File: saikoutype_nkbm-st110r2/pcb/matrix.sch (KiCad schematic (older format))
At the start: 239 parts, among them K00 CHRY_MX, K02 CHRY_MX, K03 CHRY_MX, K04 CHRY_MX, K05 CHRY_MX, K06 CHRY_MX, K07 CHRY_MX, K08 CHRY_MX, K09 CHRY_MX, K0B CHRY_MX, K0C CHRY_MX, K0D CHRY_MX, K0E CHRY_MX, K1A? CHRY_MX, K1B? CHRY_MX, K1C? CHRY_MX, K1D? CHRY_MX, K1E? CHRY_MX, K2A? CHRY_MX, K2B? CHRY_MX, K2C? CHRY_MX, K3A? CHRY_MX, K3B? CHRY_MX, K3C? CHRY_MX, K3E? CHRY_MX, K4A? CHRY_MX, K4B? CHRY_MX, K4C? CHRY_MX, K4D? CHRY_MX, K5A? CHRY_MX, K5D? CHRY_MX, K5E? CHRY_MX, K6A? CHRY_MX, K6B? CHRY_MX, K6C? CHRY_MX, K6D? CHRY_MX, K6E? CHRY_MX, K7A? CHRY_MX, K7B? CHRY_MX, K7C? CHRY_MX, K7D? CHRY_MX, K7E? CHRY_MX

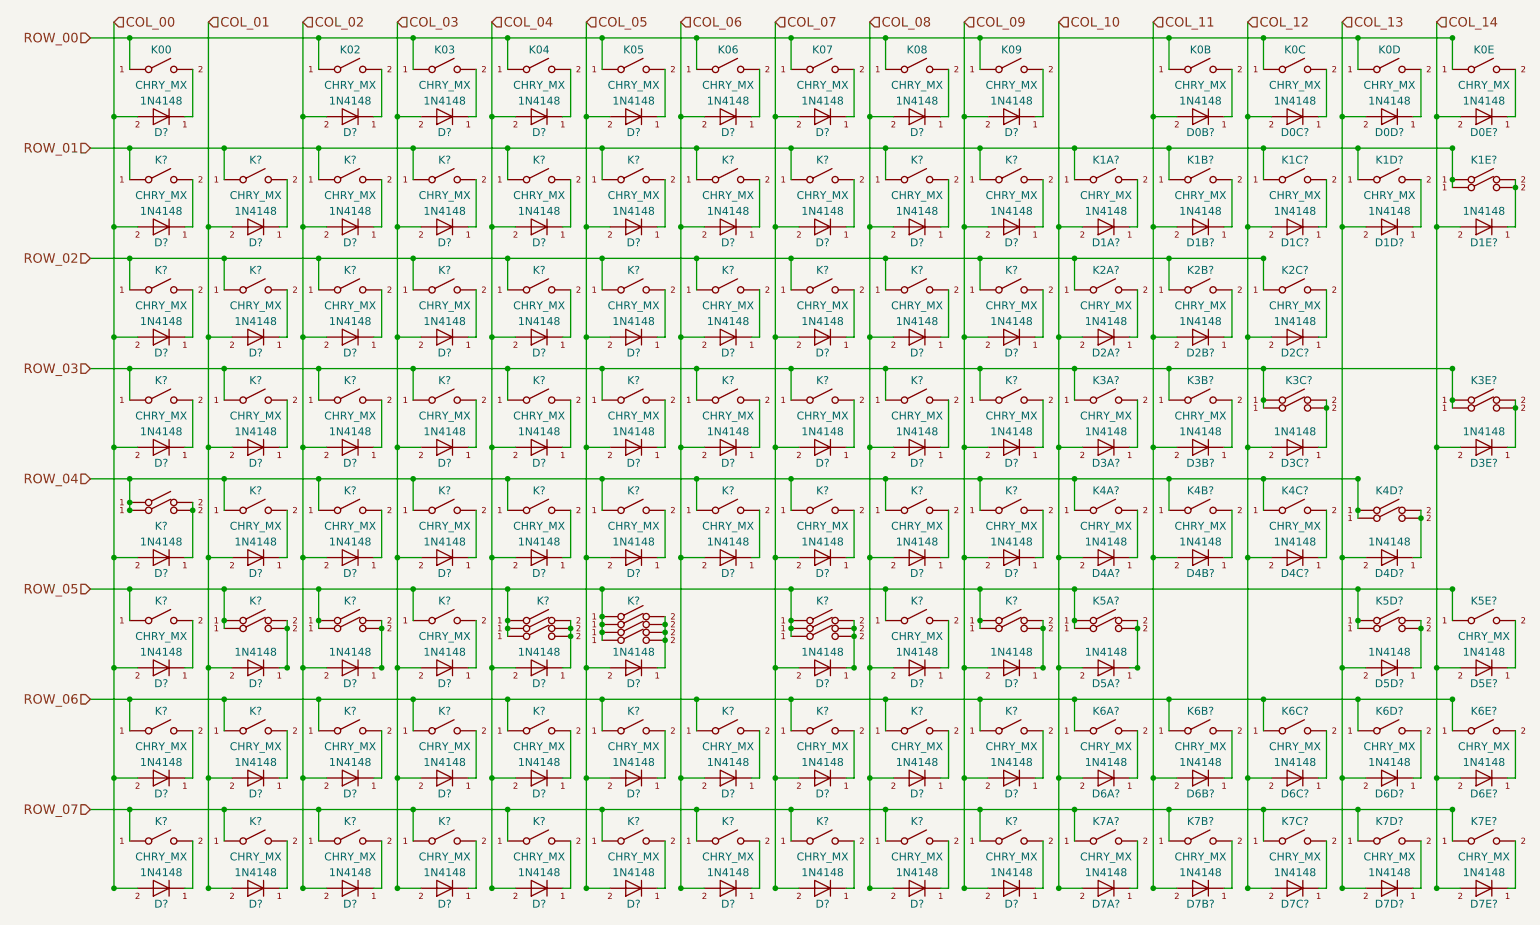
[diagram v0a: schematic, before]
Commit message: Complete reannotation of schematic and PCB.
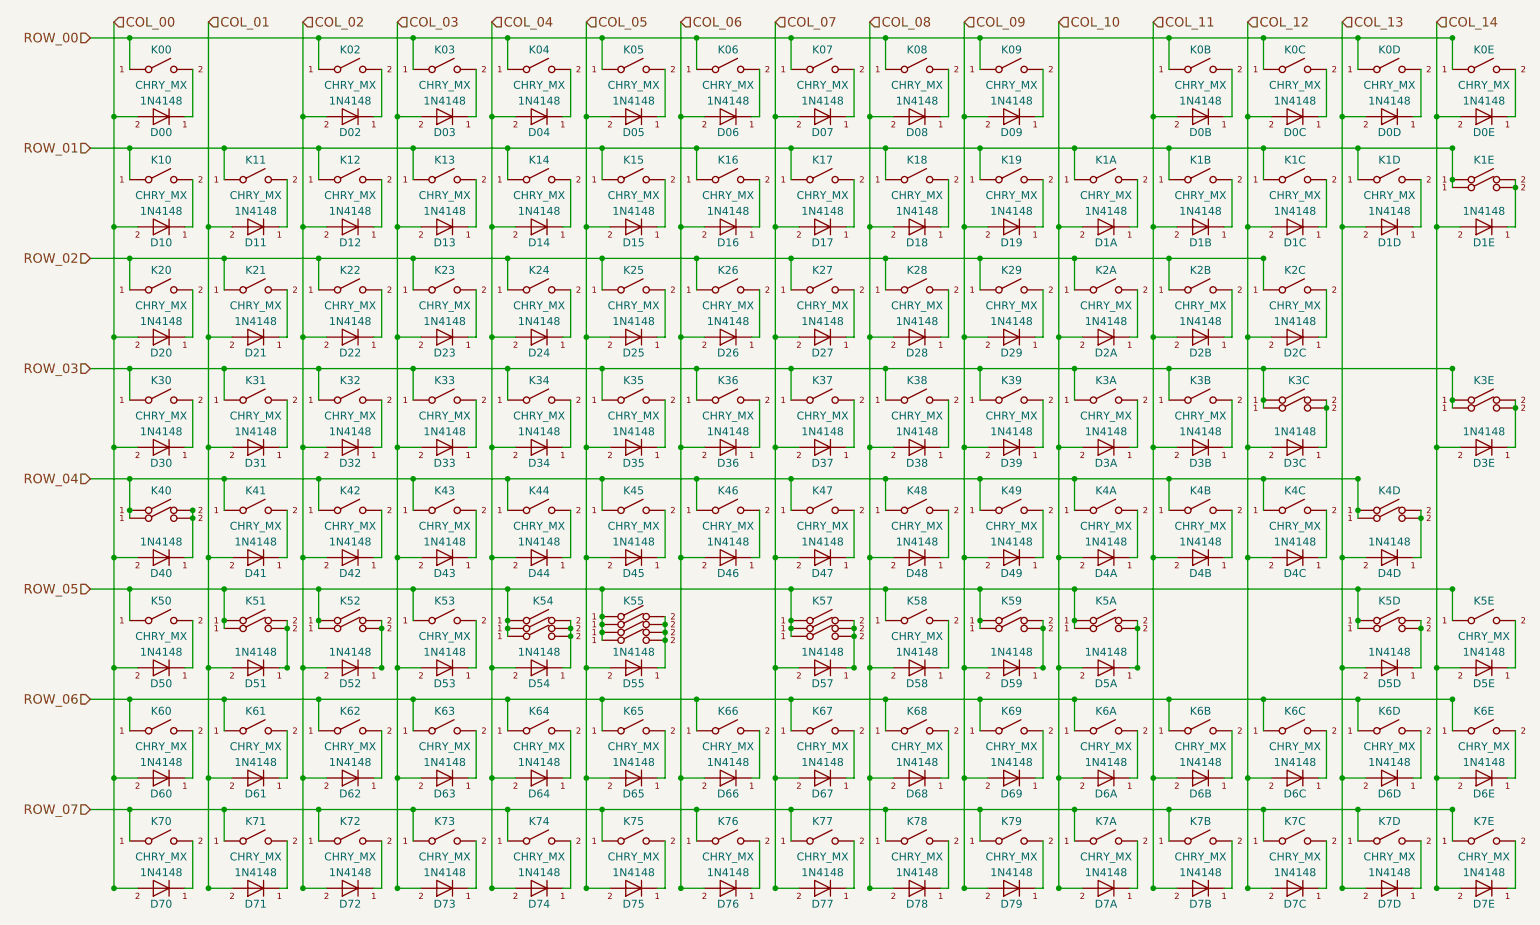
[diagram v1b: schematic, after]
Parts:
- gave numbers to parts that had none: 226
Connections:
- new net: D3C.1 (K), K3C.~ (B), K3C1.~ (B)
- new net: D1E.1 (K), K1E.~ (B), K1E1.~ (B)
- new net: D40.1 (K), K40.~ (B), K401.~ (B)
- new net: D4D.1 (K), K4D.~ (B), K4D2.~ (B)
- new net: D51.1 (K), K51.~ (B), K511.~ (B)
- new net: D52.1 (K), K52.~ (B), K521.~ (B)
- new net: D54.1 (K), K54.~ (B), K541.~ (B), K542.~ (B)
- new net: D57.1 (K), K57.~ (B), K571.~ (B), K572.~ (B)
- new net: D55.1 (K), K55.~ (B), K551.~ (B), K552.~ (B), K553.~ (B)
- new net: D59.1 (K), K59.~ (B), K591.~ (B)
- new net: D5A.1 (K), K5A.~ (B), K5A1.~ (B)
- new net: D5D.1 (K), K5D.~ (B), K5D1.~ (B)
- new net: D3E.1 (K), K3E.~ (B), K3E1.~ (B)
